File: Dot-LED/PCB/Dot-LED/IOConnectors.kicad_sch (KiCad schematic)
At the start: 2 parts, among them CON1 SJ1-3523N, P1 USB_C_Plug

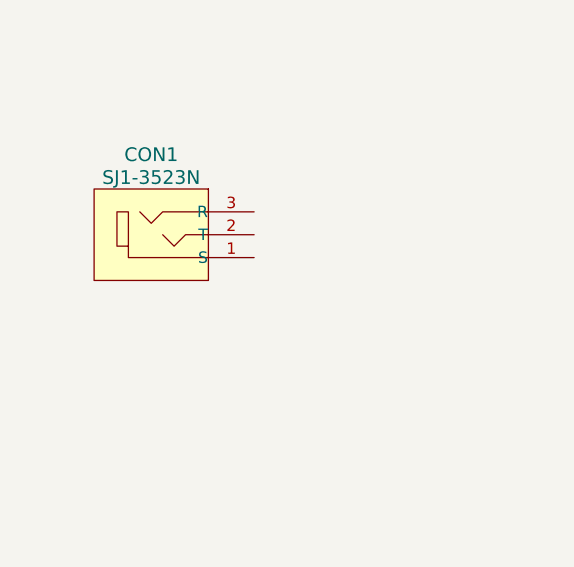
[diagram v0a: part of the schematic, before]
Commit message: add common KiCad library using plugin
https://componentsearchengine.com/ga/downloads.php
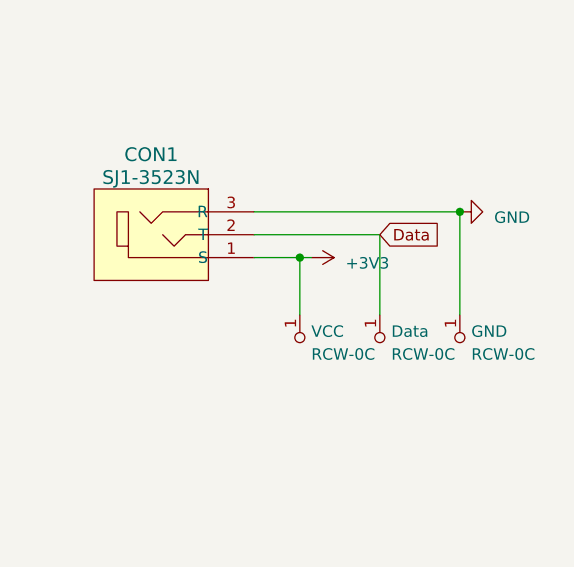
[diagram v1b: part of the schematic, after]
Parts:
- added Data, GND, VCC: RCW-0C, digikey-footprints:PROBE_PAD_1206, symbol dk_Test-Points:RCW-0C
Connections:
- net GND: now also CON1.3 (R), GND.1
- net +3V3: now reaches CON1.1 (S)
- net +3V3: now also VCC.1
- net Data: now reaches CON1.2 (T)
- net Data: now also Data.1

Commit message: Update DotLED Schem
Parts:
- added IO1, IO2, IO3, IO4, IO6, IO7, IO8, IO9: 1508-0-57-15-00-00-03-0, digikey-footprints:Test-Point-Pin_Drill2.79mm, symbol dk_Test-Points:1508-0-57-15-00-00-03-0
- P1: footprint digikey-footprints:USB_A_Female_AU-Y1006-3 -> digikey-footprints:USB-C_Female_E8124-015-01
- renumbered Data to Data1, GND to GND1, VCC to VCC1
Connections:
- net +3V3 renamed 3V3
- net Data renamed LED_Data
- new net D1: IO1.1
- new net D2: IO2.1
- new net D3: IO3.1
- new net D4: IO4.1
- new net D6: IO6.1
- new net D7: IO7.1
- new net D8: IO8.1
- new net D9: IO9.1
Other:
- moved on the sheet: GND1

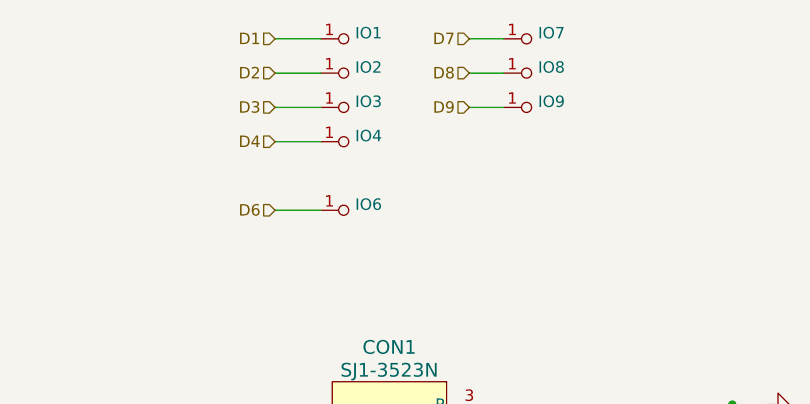
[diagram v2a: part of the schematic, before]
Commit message: update DotLED
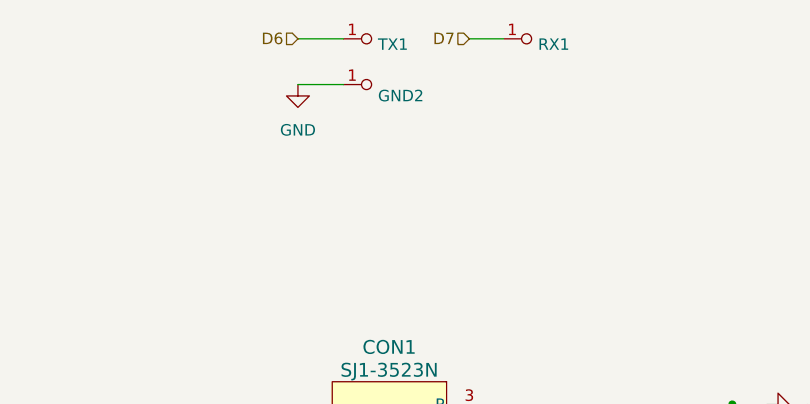
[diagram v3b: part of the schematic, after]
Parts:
- removed IO1, IO2, IO3, IO4, IO8, IO9: 1508-0-57-15-00-00-03-0, digikey-footprints:Test-Point-Pin_Drill2.79mm, symbol dk_Test-Points:1508-0-57-15-00-00-03-0
- added GND2: 1508-0-57-15-00-00-03-0, digikey-footprints:Test-Point-Pin_Drill2.79mm, symbol dk_Test-Points:1508-0-57-15-00-00-03-0
- renumbered IO7 to RX1, IO6 to TX1
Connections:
- net GND: now also GND2.1
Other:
- moved on the sheet: TX1

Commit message: Init layout for DotLED
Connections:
- net 3V3 renamed 5V
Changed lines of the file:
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@@
     (effects (font (size 1.27 1.27)) (justify right))
   )
-  (hierarchical_label "3V3" (shape input) (at 200.66 87.63 0) (fields_autoplaced)
+  (hierarchical_label "5V" (shape input) (at 200.66 87.63 0) (fields_autoplaced)
     (effects (font (size 1.27 1.27)) (justify left))
-    (property "Intersheetrefs" "${INTERSHEET_REFS}" (at 206.3109 87.63 0)
+    (property "Intersheetrefs" "${INTERSHEET_REFS}" (at 205.1014 87.63 0)
       (effects (font (size 1.27 1.27)) (justify left) hide)
     )

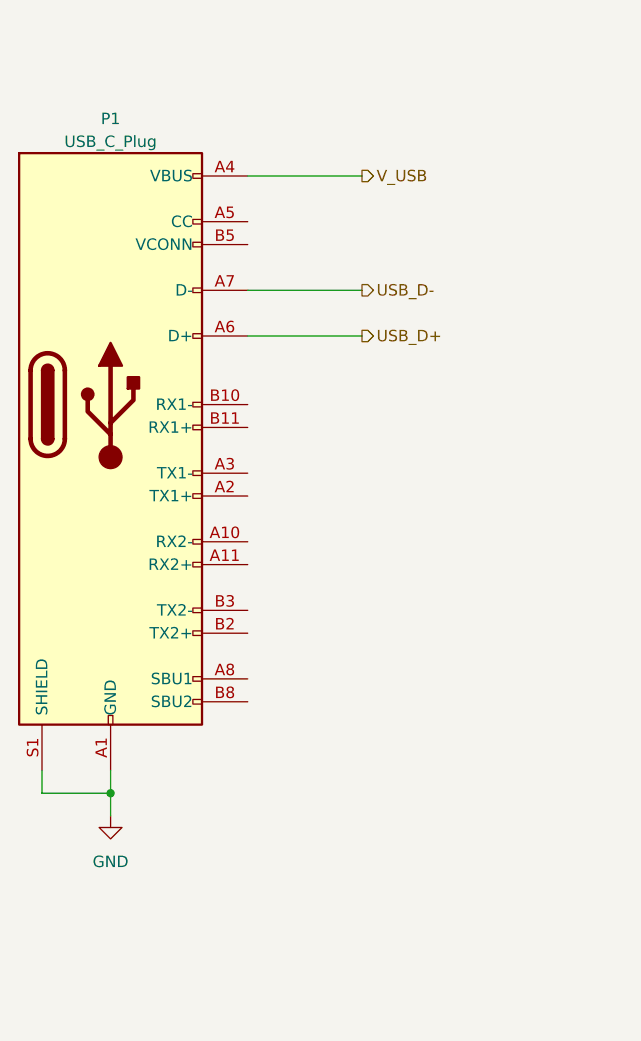
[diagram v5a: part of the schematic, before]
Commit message: finalize design based on in-stock parts
Gerber out 1.0
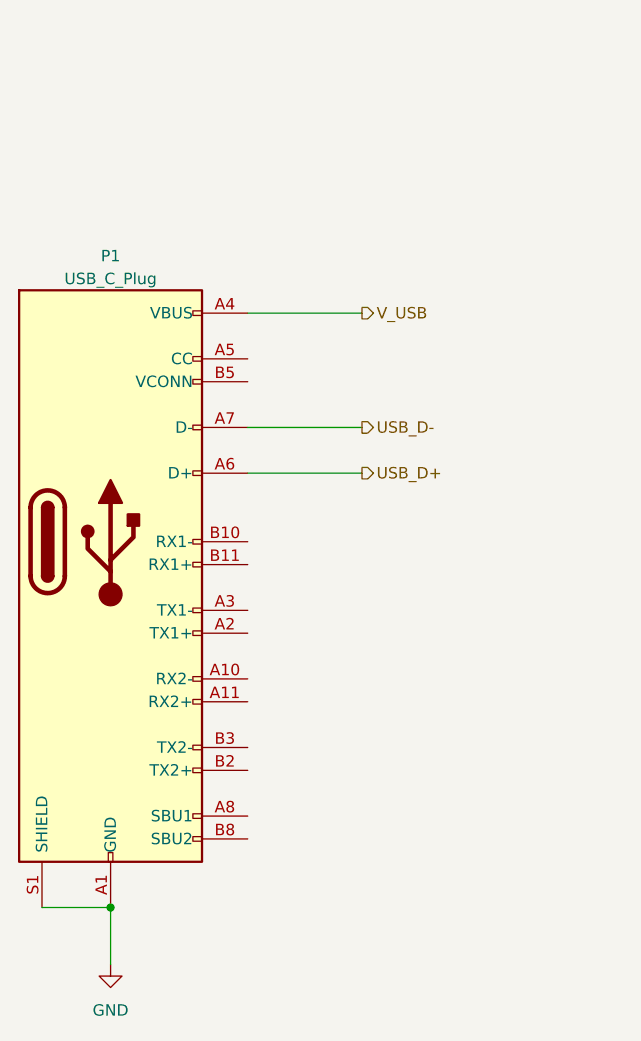
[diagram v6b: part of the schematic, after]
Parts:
- CON1: MPN SJ1-3523N -> (none)
- Data1, GND1, VCC1: MPN RCW-0C -> (none)
- GND2, RX1, TX1: MPN 1508-0-57-15-00-00-03-0 -> (none)
- P1: footprint digikey-footprints:USB-C_Female_E8124-015-01 -> Connector_USB:USB_C_Receptacle_GCT_USB4105-xx-A_16P_TopMnt_Horizontal; LCSC Part Number (none) -> C2982555
